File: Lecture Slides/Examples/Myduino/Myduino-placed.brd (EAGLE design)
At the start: 66 x 54.3 mm, 30 parts, among them J2 GENERIC-BATTERY-CONN-RECEPTAC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, Y1 16MHz

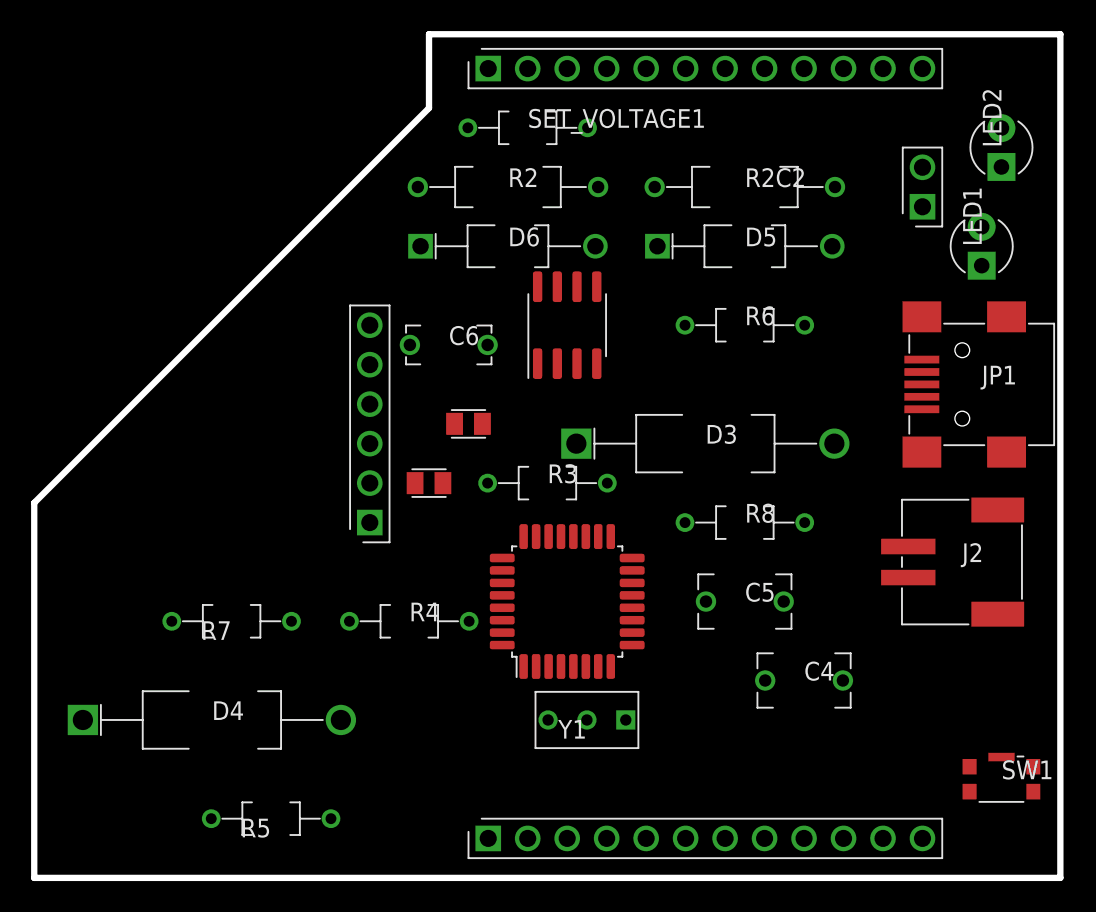
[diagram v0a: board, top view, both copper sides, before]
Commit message: gitignore.  update examples
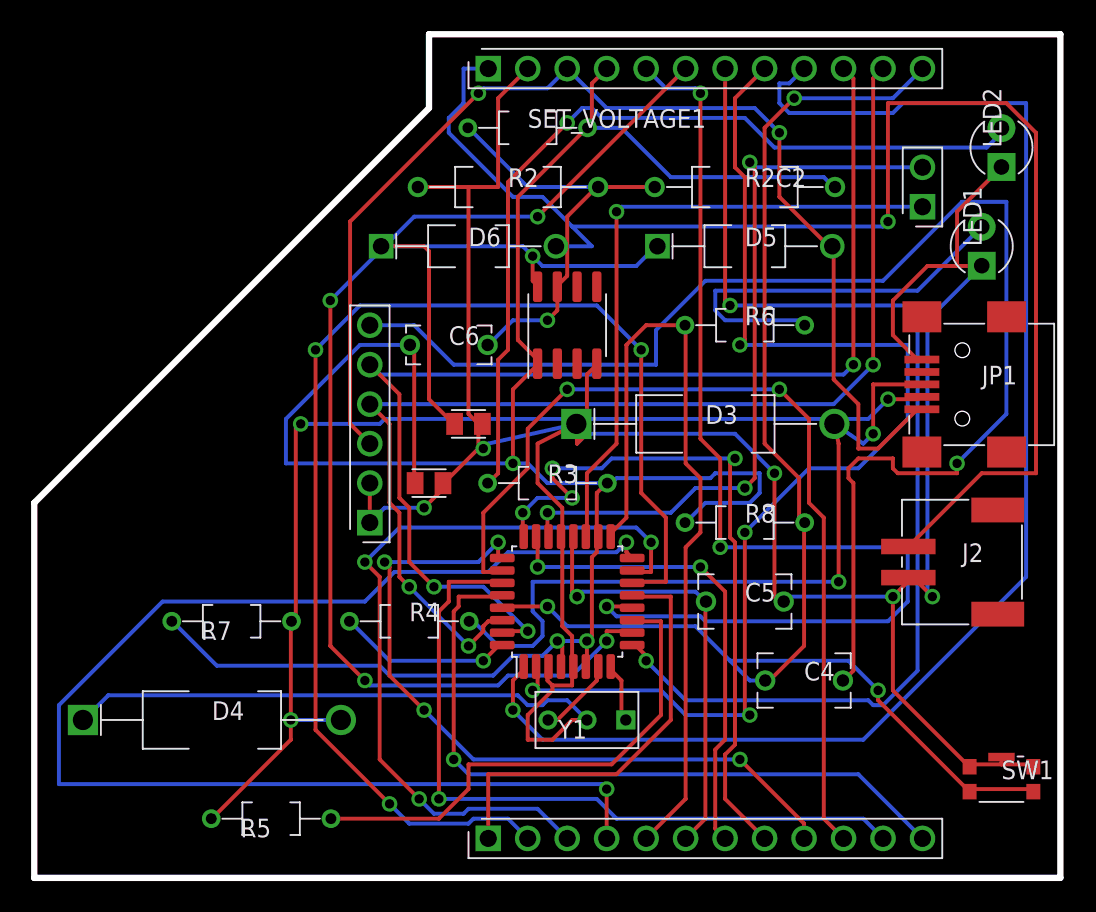
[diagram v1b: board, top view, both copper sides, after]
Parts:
- moved D6 2.54 mm to (78.7, 76.2)
- moved D3 1.27 mm to (94.0, 64.8)
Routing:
- net GND: track 0.00 -> 215.3 mm, vias 0 -> 5
- net VCC: track 0.00 -> 150.2 mm, vias 0 -> 3
- net RST: track 0.00 -> 92.0 mm, vias 0 -> 3
- net D3: track 0.00 -> 91.4 mm, vias 0 -> 1
- net VBAT: track 0.00 -> 91.1 mm, vias 0 -> 1
- net DTR/RTS: track 0.00 -> 88.5 mm, vias 0 -> 1
- net D12: track 0.00 -> 85.6 mm, vias 0 -> 2
- net D10: track 0.00 -> 82.3 mm, vias 0 -> 3
- net D4: track 0.00 -> 76.2 mm, vias 0 -> 4
- net VBUS: track 0.00 -> 76.0 mm, vias 0 -> 2
- net TXD: track 0.00 -> 75.9 mm, vias 0 -> 3
- net RXD: track 0.00 -> 74.0 mm, vias 0 -> 3
- net D6: track 0.00 -> 73.6 mm, vias 0 -> 4
- net D5: track 0.00 -> 72.0 mm, vias 0 -> 2
- net D-: track 0.00 -> 71.9 mm, vias 0 -> 3
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
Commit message: new slides
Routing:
- net VBAT: track 91.1 -> 59.3 mm, vias 1 -> 3
- net D8: track 71.4 -> 41.1 mm, vias 3 -> 2
- net D6: track 73.6 -> 44.4 mm, vias 4 -> 2
- net D13: track 51.9 -> 80.5 mm, vias 0 -> 1
- net D11: track 50.4 -> 25.0 mm, vias 3 -> 2
- net DTR/RTS: track 88.5 -> 71.2 mm, vias 1 -> 0
- net GND: track 215.3 -> 232.4 mm, vias 5 -> 6
- net D-: track 71.9 -> 88.2 mm, vias 3 -> 1
- net RXD: track 74.0 -> 90.0 mm
- net VCC: track 150.2 -> 134.6 mm, vias 3 -> 5
- net D10: track 82.3 -> 97.4 mm
- net D2: track 11.3 -> 25.0 mm, vias 1 -> 0
- net D5: track 72.0 -> 60.9 mm
- net A5: track 45.7 -> 55.7 mm, vias 1 -> 3
- net N$6: track 55.4 -> 65.0 mm, vias 1 -> 3
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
